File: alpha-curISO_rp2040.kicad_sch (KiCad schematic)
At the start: 21 parts, among them J2 SWD, U1 RP2040

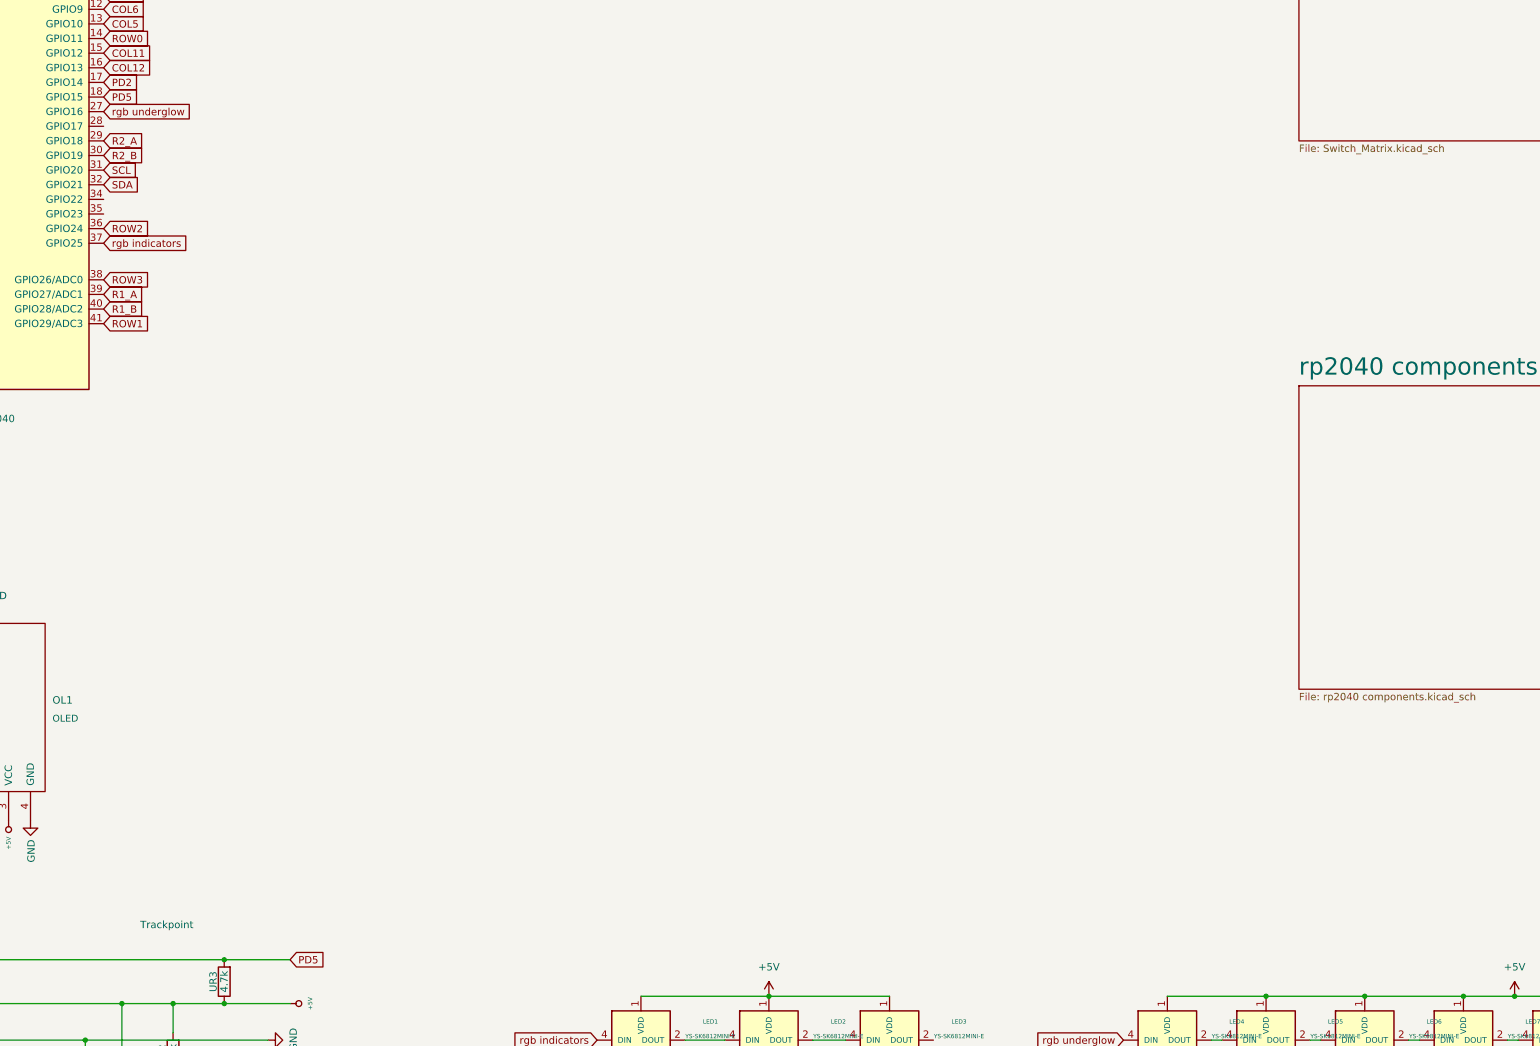
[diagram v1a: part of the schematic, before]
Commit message: added RGB components for 5v / 3v3 voltage regulation
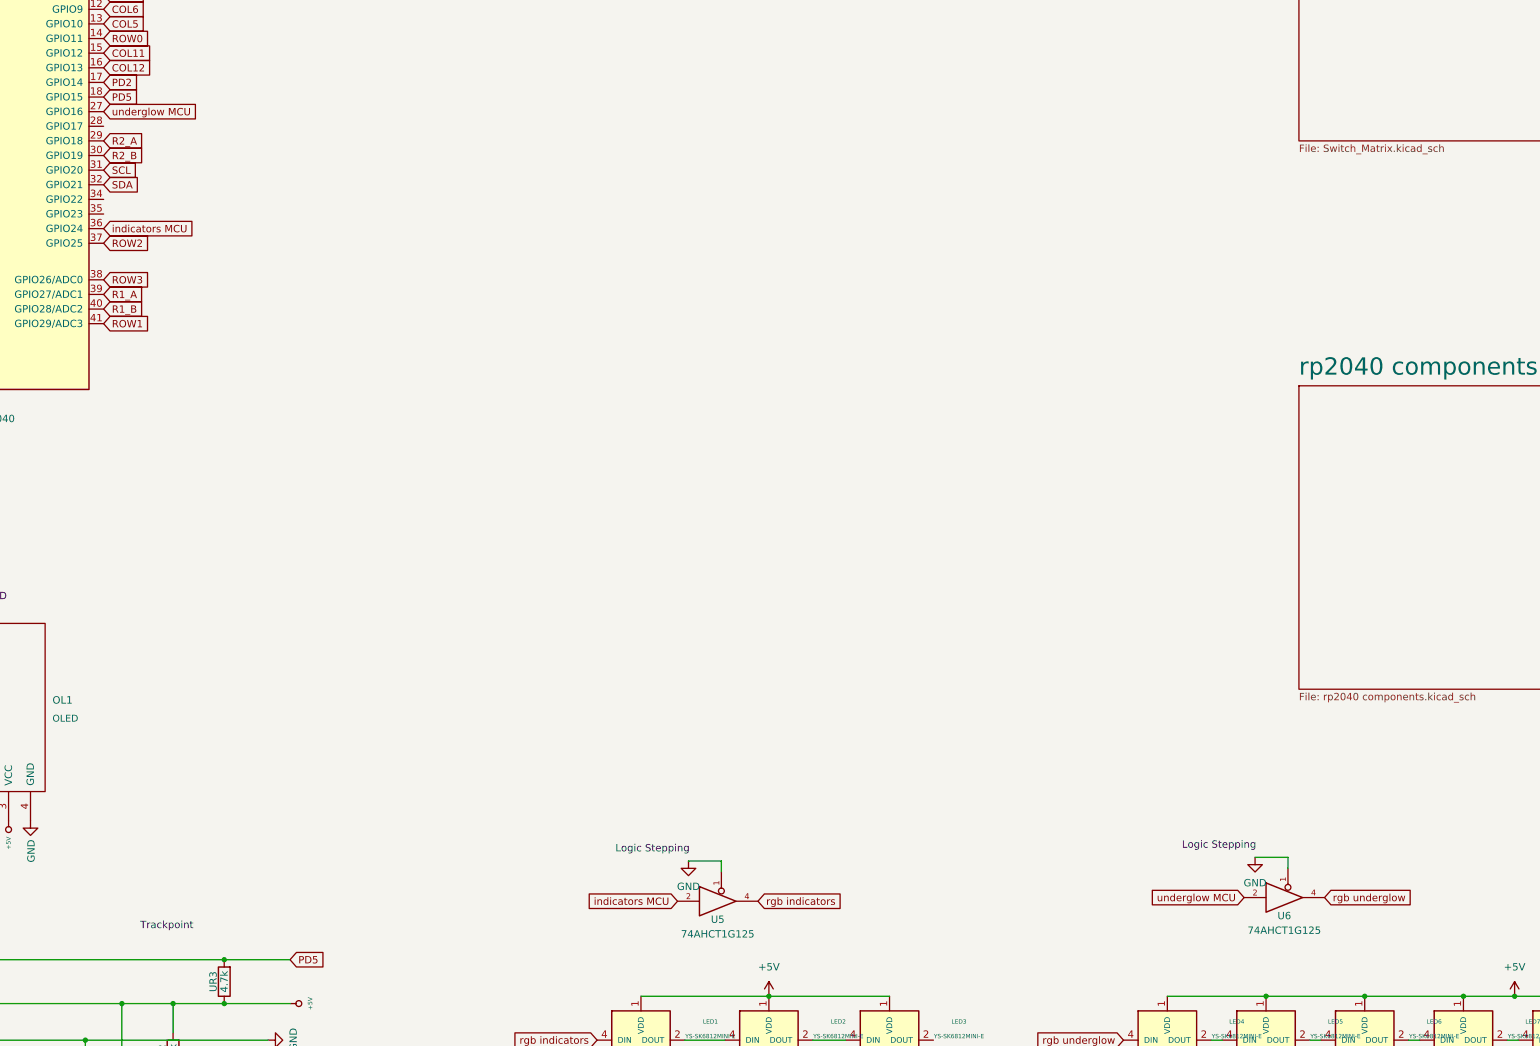
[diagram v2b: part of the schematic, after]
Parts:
- added U5, U6: 74AHCT1G125, Package_TO_SOT_SMD:SOT-23-5, symbol 74xGxx:74AHCT1G125
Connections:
- net +5V: now also U5.5 (+5V), U6.5 (+5V)
- net GND: now also U5.1, U5.3 (GND), U6.1, U6.3 (GND)
- net ROW2: now also U1.37 (GPIO25); no longer U1.36 (GPIO24)
- net rgb indicators: now also U5.4; no longer U1.37 (GPIO25)
- net rgb underglow: now also U6.4; no longer U1.27 (GPIO16)
- new net indicators MCU: U1.36 (GPIO24), U5.2
- new net underglow MCU: U1.27 (GPIO16), U6.2
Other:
- note added: "Logic Stepping"
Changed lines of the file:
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@@
+    (stroke (width 0) (type default) (color 0 0 0 0))
+  )
+  (wire (pts (xy 187.325 207.645) (xy 187.325 209.55))
     (stroke (width 0) (type default) (color 0 0 0 0))
   )
@@
     (stroke (width 0) (type default) (color 0 0 0 0))
   )
+  (wire (pts (xy 280.035 207.01) (xy 285.75 207.01))
+    (stroke (width 0) (type default) (color 0 0 0 0))
+  )
   (wire (pts (xy 264.795 246.38) (xy 281.94 246.38))
     (stroke (width 0) (type default) (color 0 0 0 0))
@@
     (stroke (width 0) (type default) (color 0 0 0 0))
   )
+  (wire (pts (xy 285.75 207.01) (xy 285.75 208.915))
+    (stroke (width 0) (type default) (color 0 0 0 0))
+  )
+  (wire (pts (xy 181.61 207.645) (xy 187.325 207.645))
+    (stroke (width 0) (type default) (color 0 0 0 0))
+  )
   (wire (pts (xy 57.785 237.49) (xy 48.895 237.49))
     (stroke (width 0) (type default) (color 0 0 0 0))
@@
     (stroke (width 0) (type default) (color 0 0 0 0))
   )
+  (text "Logic Stepping" (at 168.91 206.375 0)
+    (effects (font (size 1.27 1.27)) (justify left bottom))
+  )
   (text "Trackpoint" (at 86.36 219.71 0)
+    (effects (font (size 1.27 1.27)) (justify left bottom))
+  )
+  (text "Logic Stepping" (at 267.335 205.74 0)
     (effects (font (size 1.27 1.27)) (justify left bottom))
   )
@@
     )
   )
-  (global_label "ROW2" (shape input) (at 80.01 97.79 0) (fields_autoplaced)
-    (effects (font (size 1.27 1.27)) (justify left))
-    (property "Intersheet References" "${INTERSHEET_REFS}" (id 0) (at 87.6845 97.8694 0)
+  (global_label "underglow MCU" (shape input) (at 80.01 77.47 0) (fields_autoplaced)
+    (effects (font (size 1.27 1.27)) (justify left))
+    (property "Intersheet References" "${INTERSHEET_REFS}" (id 0) (at 97.0583 77.5494 0)
+      (effects (font (size 1.27 1.27)) (justify left) hide)
+    )
+  )
+  (global_label "ROW2" (shape input) (at 80.01 100.33 0) (fields_autoplaced)
+    (effects (font (size 1.27 1.27)) (justify left))
+    (property "Intersheet References" "${INTERSHEET_REFS}" (id 0) (at 87.6845 100.4094 0)
       (effects (font (size 1.27 1.27)) (justify left) hide)
     )
@@
     )
   )
+  (global_label "underglow MCU" (shape input) (at 278.13 213.995 180) (fields_autoplaced)
+    (effects (font (size 1.27 1.27)) (justify right))
+    (property "Intersheet References" "${INTERSHEET_REFS}" (id 0) (at 261.0817 213.9156 0)
+      (effects (font (size 1.27 1.27)) (justify right) hide)
+    )
+  )
   (global_label "XTAL_IN" (shape input) (at 39.37 60.96 180) (fields_autoplaced)
     (effects (font (size 1.27 1.27)) (justify right))
@@
     )
   )
-  (global_label "rgb underglow" (shape input) (at 80.01 77.47 0) (fields_autoplaced)
-    (effects (font (size 1.27 1.27)) (justify left))
-    (property "Intersheet References" "${INTERSHEET_REFS}" (id 0) (at 96.0907 77.5494 0)
-      (effects (font (size 1.27 1.27)) (justify left) hide)
-    )
-  )
   (global_label "QSPI_CLK" (shape input) (at 39.37 101.6 180) (fields_autoplaced)
     (effects (font (size 1.27 1.27)) (justify right))
@@
     )
   )
+  (global_label "rgb underglow" (shape input) (at 292.1 213.995 0) (fields_autoplaced)
+    (effects (font (size 1.27 1.27)) (justify left))
+    (property "Intersheet References" "${INTERSHEET_REFS}" (id 0) (at 308.1807 214.0744 0)
+      (effects (font (size 1.27 1.27)) (justify left) hide)
+    )
+  )
   (global_label "CS" (shape input) (at 39.37 99.06 180) (fields_autoplaced)
     (effects (font (size 1.27 1.27)) (justify right))
@@
     )
   )
+  (global_label "rgb indicators" (shape input) (at 193.675 214.63 0) (fields_autoplaced)
+    (effects (font (size 1.27 1.27)) (justify left))
+    (property "Intersheet References" "${INTERSHEET_REFS}" (id 0) (at 209.5743 214.7094 0)
+      (effects (font (size 1.27 1.27)) (justify left) hide)
+    )
+  )
+  (global_label "indicators MCU" (shape input) (at 179.705 214.63 180) (fields_autoplaced)
+    (effects (font (size 1.27 1.27)) (justify right))
+    (property "Intersheet References" "${INTERSHEET_REFS}" (id 0) (at 162.8381 214.5506 0)
+      (effects (font (size 1.27 1.27)) (justify right) hide)
+    )
+  )
   (global_label "XTAL_OUT" (shape input) (at 39.37 66.04 180) (fields_autoplaced)
     (effects (font (size 1.27 1.27)) (justify right))
@@
     )
   )
-  (global_label "rgb indicators" (shape input) (at 80.01 100.33 0) (fields_autoplaced)
-    (effects (font (size 1.27 1.27)) (justify left))
-    (property "Intersheet References" "${INTERSHEET_REFS}" (id 0) (at 95.9093 100.4094 0)
-      (effects (font (size 1.27 1.27)) (justify left) hide)
-    )
-  )
   (global_label "PD5" (shape input) (at 80.01 74.93 0) (fields_autoplaced)
     (effects (font (size 1.27 1.27)) (justify left))
@@
     (effects (font (size 1.27 1.27)) (justify left))
     (property "Intersheet References" "${INTERSHEET_REFS}" (id 0) (at 87.1402 111.8394 0)
+      (effects (font (size 1.27 1.27)) (justify left) hide)
+    )
+  )
+  (global_label "indicators MCU" (shape input) (at 80.01 97.79 0) (fields_autoplaced)
+    (effects (font (size 1.27 1.27)) (justify left))
+    (property "Intersheet References" "${INTERSHEET_REFS}" (id 0) (at 96.8769 97.8694 0)
       (effects (font (size 1.27 1.27)) (justify left) hide)
     )
@@
     (pin "1")
     (pin "2")
+  )
+  (symbol (lib_id "74xGxx:74AHCT1G125") (at 187.325 214.63 0) (unit 1)
+    (in_bom yes) (on_board yes)
+    (property "Reference" "U5" (id 0) (at 186.69 217.805 0))
+    (property "Value" "74AHCT1G125" (id 1) (at 186.69 220.345 0))
+    (property "Footprint" "Package_TO_SOT_SMD:SOT-23-5" (id 2) (at 187.325 214.63 0)
+      (effects (font (size 1.27 1.27)) hide)
+    )
+    (property "Datasheet" "http://www.ti.com/lit/sg/scyt129e/scyt129e.pdf" (id 3) (at 188.595 226.06 0)
+      (effects (font (size 1.27 1.27)) hide)
+    )
+    (pin "1")
+    (pin "2")
+    (pin "3")
+    (pin "4")
+    (pin "5")
   )
   (symbol (lib_id "power:GND") (at 108.585 238.76 90) (unit 1)
@@
     (pin "3")
     (pin "4")
+  )
+  (symbol (lib_id "power:GND") (at 181.61 207.645 0) (unit 1)
+    (in_bom yes) (on_board yes) (fields_autoplaced)
+    (property "Reference" "#PWR0144" (id 0) (at 181.61 213.995 0)
+      (effects (font (size 1.27 1.27)) hide)
+    )
+    (property "Value" "GND" (id 1) (at 181.61 212.09 0))
+    (property "Footprint" "" (id 2) (at 181.61 207.645 0)
+      (effects (font (size 1.27 1.27)) hide)
+    )
+    (property "Datasheet" "" (id 3) (at 181.61 207.645 0)
+      (effects (font (size 1.27 1.27)) hide)
+    )
+    (pin "1")
   )
   (symbol (lib_id "power:+1V1") (at 34.29 85.09 0) (unit 1)
@@
     (pin "1")
   )
+  (symbol (lib_id "74xGxx:74AHCT1G125") (at 285.75 213.995 0) (unit 1)
+    (in_bom yes) (on_board yes)
+    (property "Reference" "U6" (id 0) (at 285.115 217.17 0))
+    (property "Value" "74AHCT1G125" (id 1) (at 285.115 219.71 0))
+    (property "Footprint" "Package_TO_SOT_SMD:SOT-23-5" (id 2) (at 285.75 213.995 0)
+      (effects (font (size 1.27 1.27)) hide)
+    )
+    (property "Datasheet" "http://www.ti.com/lit/sg/scyt129e/scyt129e.pdf" (id 3) (at 287.02 225.425 0)
+      (effects (font (size 1.27 1.27)) hide)
+    )
+    (pin "1")
+    (pin "2")
+    (pin "3")
+    (pin "4")
+    (pin "5")
+  )
   (symbol (lib_id "power:+5V") (at 325.12 231.14 0) (unit 1)
     (in_bom yes) (on_board yes) (fields_autoplaced)
@@
     (pin "2")
   )
+  (symbol (lib_id "power:GND") (at 280.035 207.01 0) (unit 1)
+    (in_bom yes) (on_board yes) (fields_autoplaced)
+    (property "Reference" "#PWR0145" (id 0) (at 280.035 213.36 0)
+      (effects (font (size 1.27 1.27)) hide)
+    )
+    (property "Value" "GND" (id 1) (at 280.035 211.455 0))
+    (property "Footprint" "" (id 2) (at 280.035 207.01 0)
+      (effects (font (size 1.27 1.27)) hide)
+    )
+    (property "Datasheet" "" (id 3) (at 280.035 207.01 0)
+      (effects (font (size 1.27 1.27)) hide)
+    )
+    (pin "1")
+  )
   (symbol (lib_id "Device:R_Small") (at 34.036 50.8 90) (unit 1)
     (in_bom yes) (on_board yes) (fields_autoplaced)
@@
       (reference "#PWR0143") (unit 1) (value "GND") (footprint "")
     )
+    (path "/517913b4-c4b7-482a-b8a5-840d40210333"
+      (reference "#PWR0144") (unit 1) (value "GND") (footprint "")
+    )
+    (path "/c78a29ac-a3af-46b8-814d-36d80849f4d4"
+      (reference "#PWR0145") (unit 1) (value "GND") (footprint "")
+    )
     (path "/ed815977-8ce9-43bf-9f7d-c601496617ea/a29ce2bd-7f3e-4f4b-b2fc-e02b47b0b88b"
       (reference "#PWR0147") (unit 1) (value "GND") (footprint "")
@@
       (reference "U4") (unit 1) (value "USBLC6-2SC6") (footprint "Package_TO_SOT_SMD:SOT-23-6")
     )
+    (path "/12a4f8fa-3f32-4827-b285-250d7a632ebf"
+      (reference "U5") (unit 1) (value "74AHCT1G125") (footprint "Package_TO_SOT_SMD:SOT-23-5")
+    )
+    (path "/a83007ac-9918-4699-b2ee-5a09f1e2d154"
+      (reference "U6") (unit 1) (value "74AHCT1G125") (footprint "Package_TO_SOT_SMD:SOT-23-5")
+    )
     (path "/af43070d-a454-4404-b870-a8fc6185c621"

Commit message: tiny schematics clean up
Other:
- note removed: "does the rgb have to be powered bz 5v or can it be powered by 3v3?"
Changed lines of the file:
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@@
-    (effects (font (size 1.27 1.27)) (justify left bottom))
-  )
-  (text "does the rgb have to be powered bz 5v or can it be powered by\n 3v3?"
-    (at 163.195 253.365 0)
     (effects (font (size 1.27 1.27)) (justify left bottom))
   )

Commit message: rgb schematics
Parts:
- removed U6: 74AHCT1G125, Package_TO_SOT_SMD:SOT-23-5, symbol 74xGxx:74AHCT1G125
- added C19: 100nF, Capacitor_SMD:C_0402_1005Metric, symbol Device:C_Small
- U5: footprint Package_TO_SOT_SMD:SOT-23-5 -> Package_TO_SOT_SMD:TSOT-23-5
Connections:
- net +5V: now also C19.2
- net GND: now also C19.1
- net rgb indicators: now also LED11.2 (DOUT); no longer U5.4
- net rgb underglow: now also U5.4
- net indicators MCU: no longer names the net of U1.36 (GPIO24)
- net indicators MCU: no longer U5.2
- net underglow MCU renamed RGB MCU
- net RGB MCU: now also U5.2
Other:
- note added: "4 pins free! we can reconnect the rotaries"
- note removed: "Logic Stepping"
- moved on the sheet: LED1, LED10, LED11, LED2, LED3, LED4, LED5, LED6, LED7, LED8, LED9
